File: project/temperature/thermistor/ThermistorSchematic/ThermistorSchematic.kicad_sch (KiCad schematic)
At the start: 12 parts, among them U1 MCP601, U2 MCP601

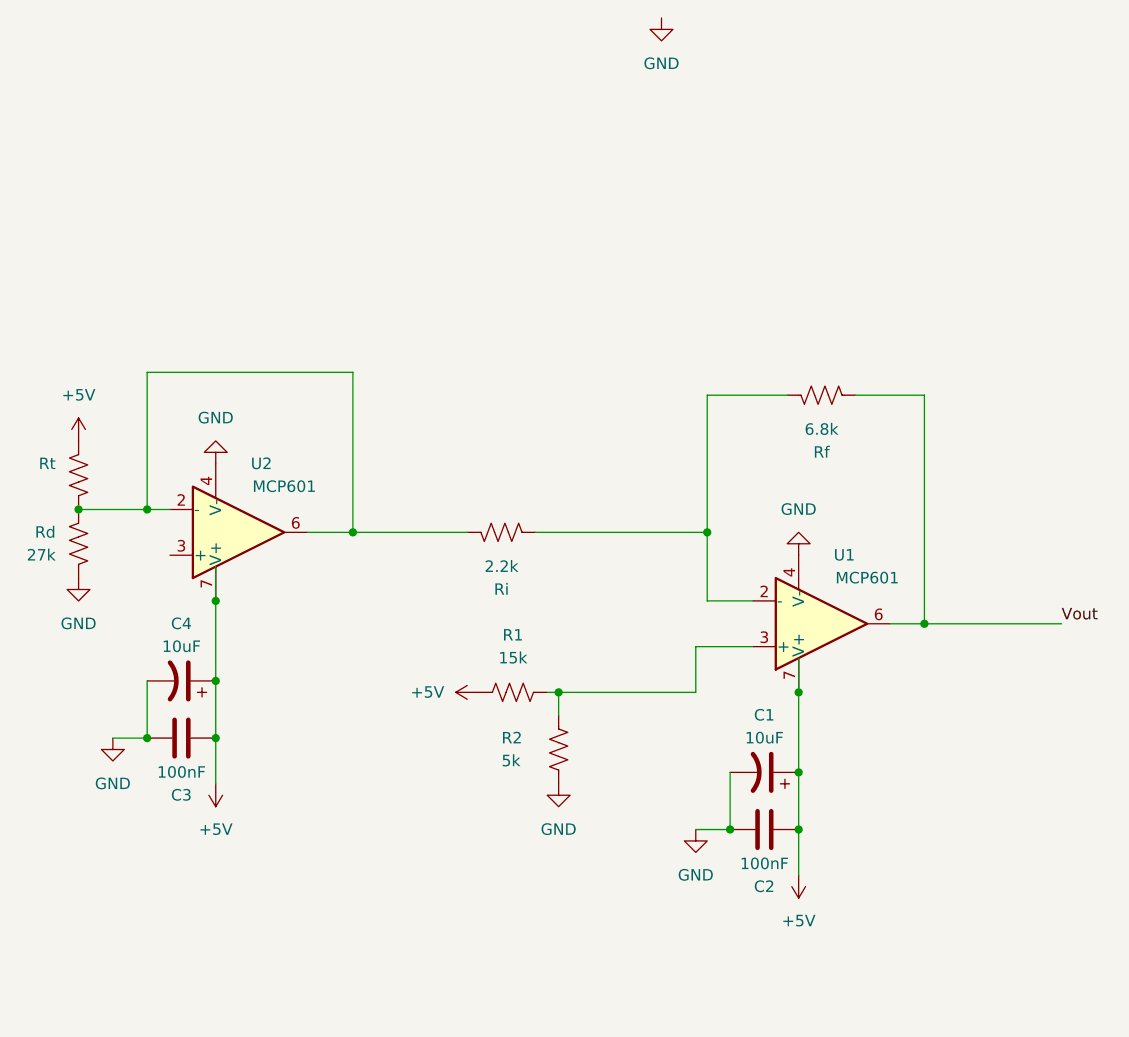
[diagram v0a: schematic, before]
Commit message: update schematic
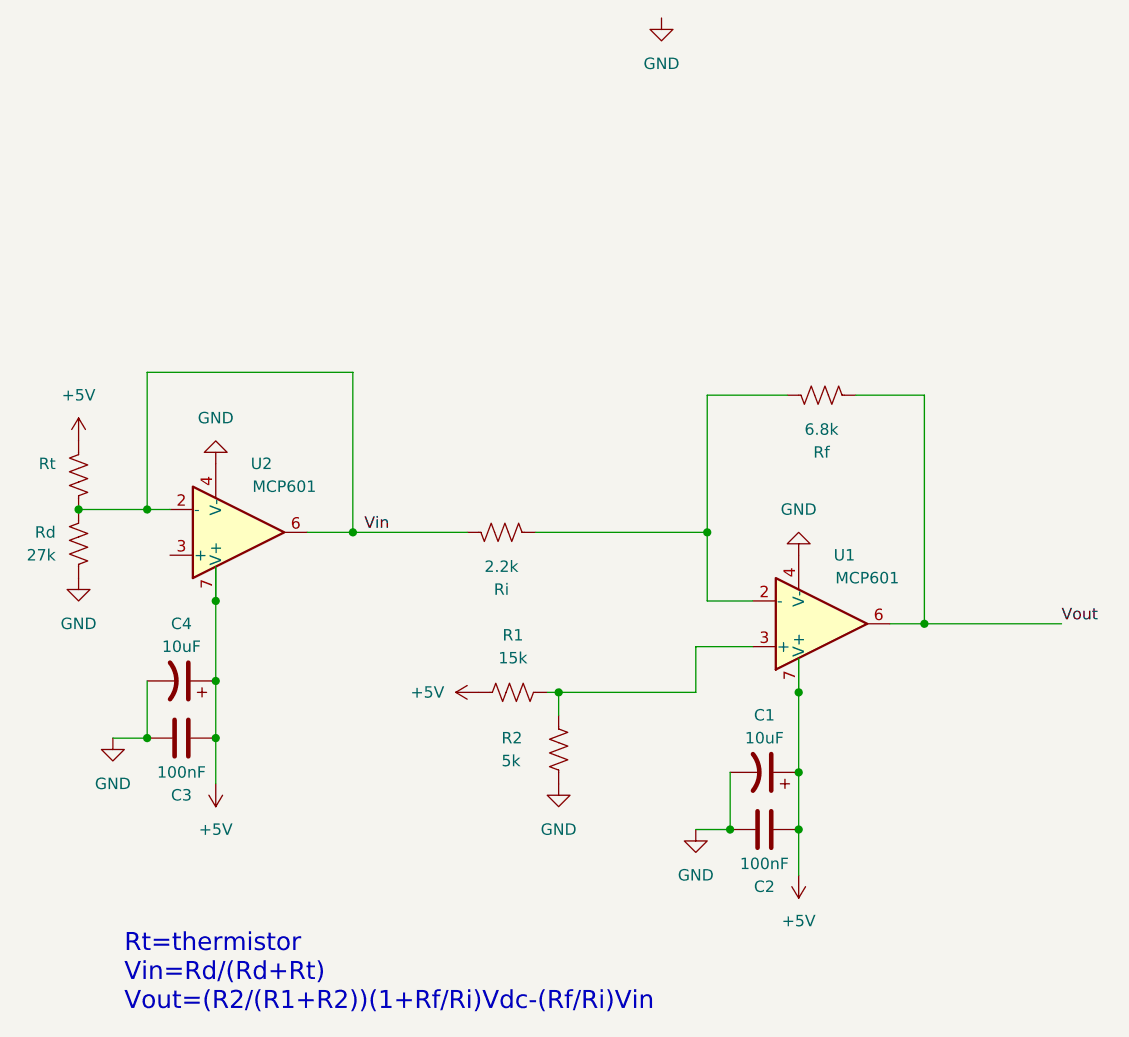
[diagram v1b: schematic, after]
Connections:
- net Vin: now reaches Rd.1, Ri.1, Rt.2, U2.2 (-), U2.6
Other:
- note added: "Rt=thermistor Vin=Rd/(Rd+Rt) Vout=(R2/(R1+R2))(1+Rf/Ri)Vdc-(Rf/Ri)Vin"
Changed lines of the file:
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@@
     (stroke (width 0) (type default))
+  )
+  (text "Rt=thermistor\nVin=Rd/(Rd+Rt)\nVout=(R2/(R1+R2))(1+Rf/Ri)Vdc-(Rf/Ri)Vin"
+    (at 91.44 147.32 0)
+    (effects (font (size 2 2)) (justify left bottom))
+  )
+  (label "Vin" (at 118.11 93.98 0) (fields_autoplaced)
+    (effects (font (size 1.27 1.27)) (justify left bottom))
   )
   (label "Vout" (at 195.58 104.14 0) (fields_autoplaced)

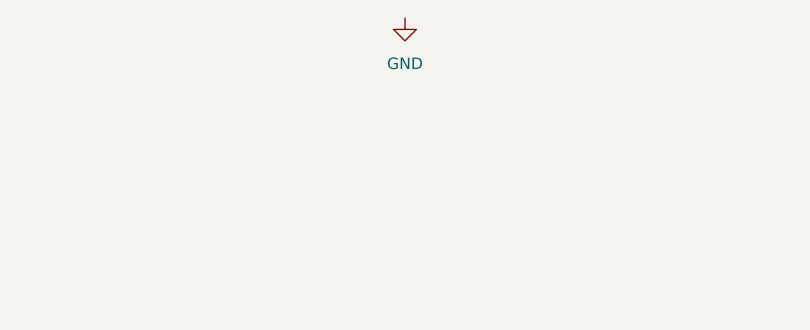
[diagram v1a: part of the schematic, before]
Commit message: Clean up schematic
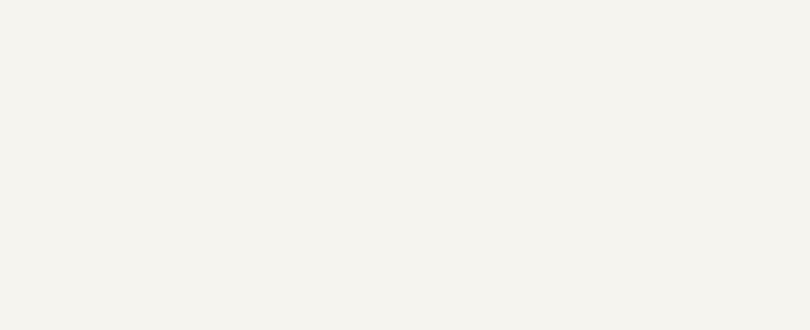
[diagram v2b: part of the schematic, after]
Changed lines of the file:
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@@
-    )
-  )
-  (symbol (lib_id "power:GND") (at 151.13 36.83 0) (unit 1)
-    (in_bom yes) (on_board yes) (dnp no) (fields_autoplaced)
-    (property "Reference" "#PWR05" (at 151.13 43.18 0)
-      (effects (font (size 1.27 1.27)) hide)
-    )
-    (property "Value" "GND" (at 151.13 41.91 0)
-      (effects (font (size 1.27 1.27)))
-    )
-    (property "Footprint" "" (at 151.13 36.83 0)
-      (effects (font (size 1.27 1.27)) hide)
-    )
-    (property "Datasheet" "" (at 151.13 36.83 0)
-      (effects (font (size 1.27 1.27)) hide)
-    )
-    (pin "1")
-    (instances
-      (project "ThermistorSchematic"
-        (path "/8bafe1b0-6793-4df3-8ff4-47084f629b8f"
-          (reference "#PWR05") (unit 1)
-        )
-      )
     )
   )
